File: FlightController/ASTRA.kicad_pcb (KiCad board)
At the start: 2 copper layers, 66 x 77.5 mm, 42 parts

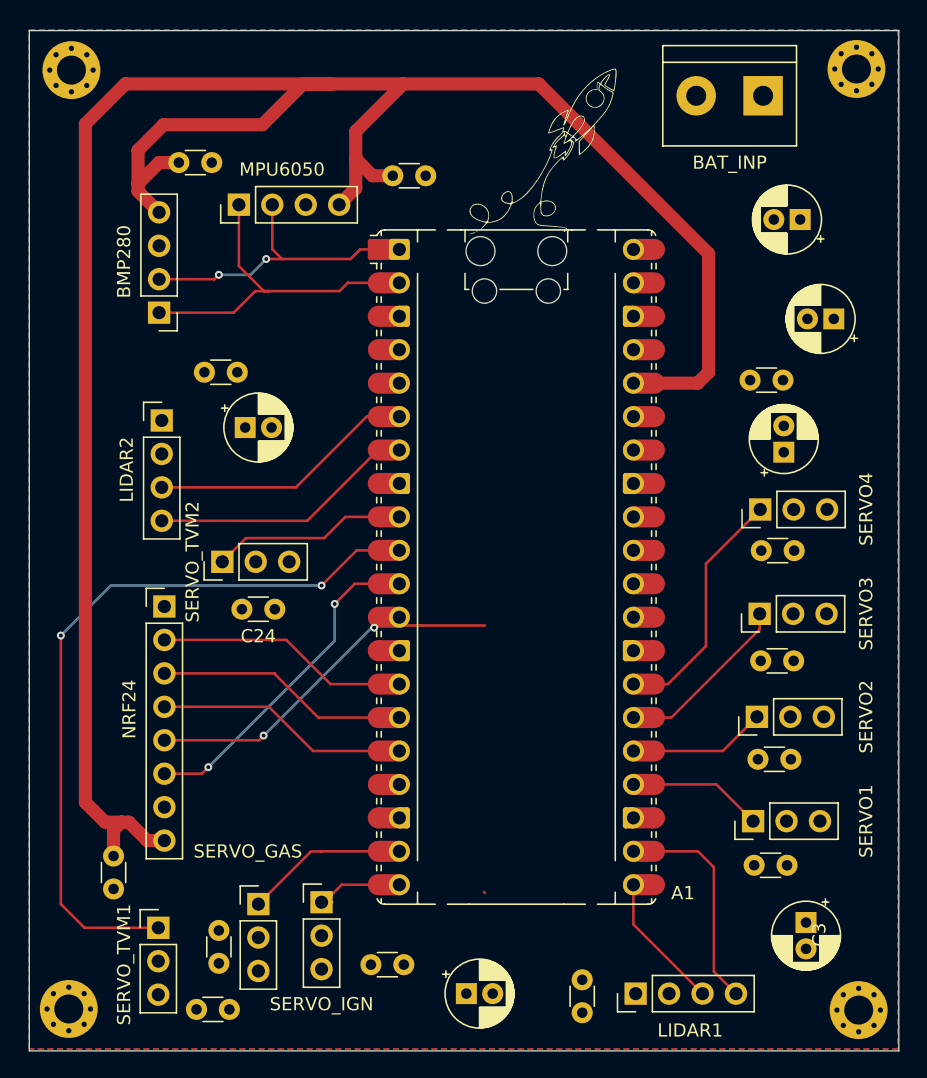
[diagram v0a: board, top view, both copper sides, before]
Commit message: added new flight controller pcb files
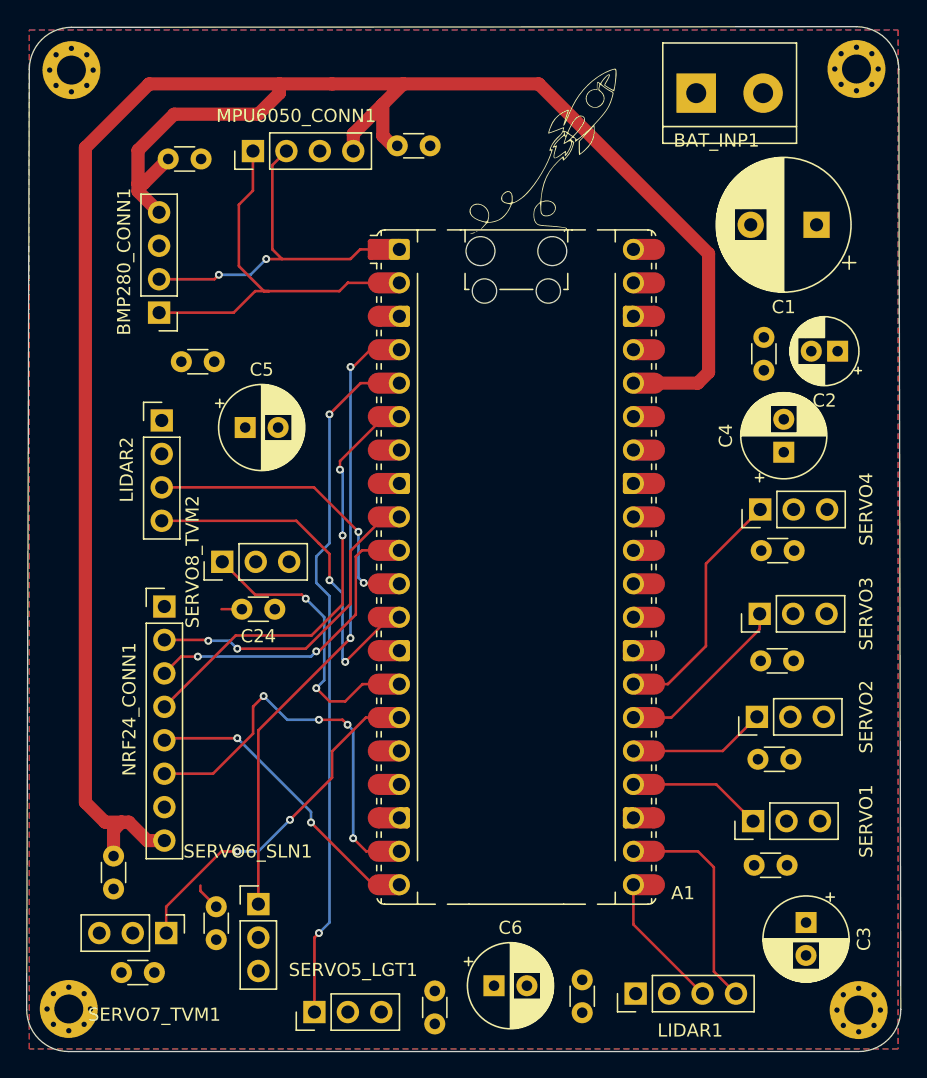
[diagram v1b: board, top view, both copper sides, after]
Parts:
- removed the C4 at (142.0, 121.4)
- added C6: 100uf, Capacitor_THT:CP_Radial_D6.3mm_P2.50mm, F.Cu at (144.1, 120.8)
- C1: footprint Capacitor_THT:CP_Radial_D5.0mm_P2.00mm -> Capacitor_THT:CP_Radial_D10.0mm_P5.00mm
- C3, C4, C5: footprint Capacitor_THT:CP_Radial_D5.0mm_P2.00mm -> Capacitor_THT:CP_Radial_D6.3mm_P2.50mm
- moved G*** 18.0 mm to (138.2, 72.5)
- moved SERVO5_LGT1 8.36 mm to (130.5, 122.8), turned to 90 degrees
- moved C23 6.35 mm to (118.3, 119.8)
- moved BAT_INP1 5.08 mm to (159.5, 53.0), turned to 0 degrees
- moved MPU6050_CONN1 4.21 mm to (125.8, 57.4)
- moved C16 3.09 mm to (139.6, 121.2), turned to -90 degrees
- moved C2 2.47 mm to (170.2, 72.6)
- moved C11 2.30 mm to (139.2, 57.0)
- moved C14 1.92 mm to (122.8, 73.4)
- moved C15 1.81 mm to (123.0, 117.3)
- moved C1 1.31 mm to (168.6, 63.0)
- moved C22 1.29 mm to (164.6, 74.0), turned to 90 degrees
- moved C12 0.86 mm to (121.8, 58.0)
- moved SERVO7_TVM1 0.72 mm to (119.2, 116.8), turned to -90 degrees
- renumbered BAT_INP to BAT_INP1, BMP280 to BMP280_CONN1, MPU6050 to MPU6050_CONN1, NRF24 to NRF24_CONN1, SERVO_IGN to SERVO5_LGT1, SERVO_GAS to SERVO6_SLN1, SERVO_TVM1 to SERVO7_TVM1, SERVO_TVM2 to SERVO8_TVM2
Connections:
- A1 pad 10: /SERVO7_TVM -> /MOSI
- A1 pad 11: /CE -> /RCV_L2
- A1 pad 12: /CSN -> /XMIT_L2
- A1 pad 14: /SCK -> /SERVO8_TVM
- A1 pad 15: /MOSI -> /SERVO7_TVM
- A1 pad 16: /MISO -> unconnected-(A1-GPIO12-Pad16)
- A1 pad 17: /GPIO_NCH -> unconnected-(A1-GPIO13-Pad17)
- A1 pad 19: /SERVO6_SLN -> /CE
- A1 pad 20: /SERVO5_LGT -> /CSN
- A1 pad 29: /GPIO_SLN -> unconnected-(A1-GPIO22-Pad29)
- A1 pad 4: unconnected-(A1-GPIO2-Pad4) -> /SERVO6_SLN
- A1 pad 5: unconnected-(A1-GPIO3-Pad5) -> /SERVO5_LGT
- A1 pad 6: /RCV_L2 -> /MISO
- A1 pad 7: /XMIT_L2 -> unconnected-(A1-GPIO5-Pad7)
- A1 pad 9: /SERVO8_TVM -> /SCK
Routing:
- net /SERVO5_LGT: track 7.40 -> 53.0 mm, vias 0 -> 2
- net /SERVO6_SLN: track 12.4 -> 48.0 mm, vias 0 -> 2
- net /SERVO7_TVM: track 56.9 -> 26.8 mm
- net /MISO: track 19.2 -> 33.7 mm, vias 0 -> 2
- net /3v3: track 171.3 -> 161.9 mm
- net /SERVO8_TVM: track 14.1 -> 22.4 mm, vias 0 -> 2
- net /XMIT_L2: track 20.3 -> 28.0 mm, vias 0 -> 2
- net /CE: track 25.5 -> 31.2 mm, vias 2 -> 4
- net /SCK: track 19.2 -> 24.6 mm, vias 0 -> 2
- net /MOSI: track 19.3 -> 24.3 mm, vias 0 -> 2
- net /CSN: track 28.0 -> 23.0 mm
- net /SCL_MPU: track 26.9 -> 31.4 mm
- net /SDA_MPU: track 23.6 -> 28.1 mm
- net /5V: track 0.00 -> 3.65 mm
- net /RCV_L2: track 20.3 -> 23.1 mm, vias 0 -> 2
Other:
- board size 66 x 77.5 mm -> 66.4 x 77.8 mm
- rule pad_to_mask_clearance: 0.05 -> 0
